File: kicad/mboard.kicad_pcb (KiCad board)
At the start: 2 copper layers, 3 parts

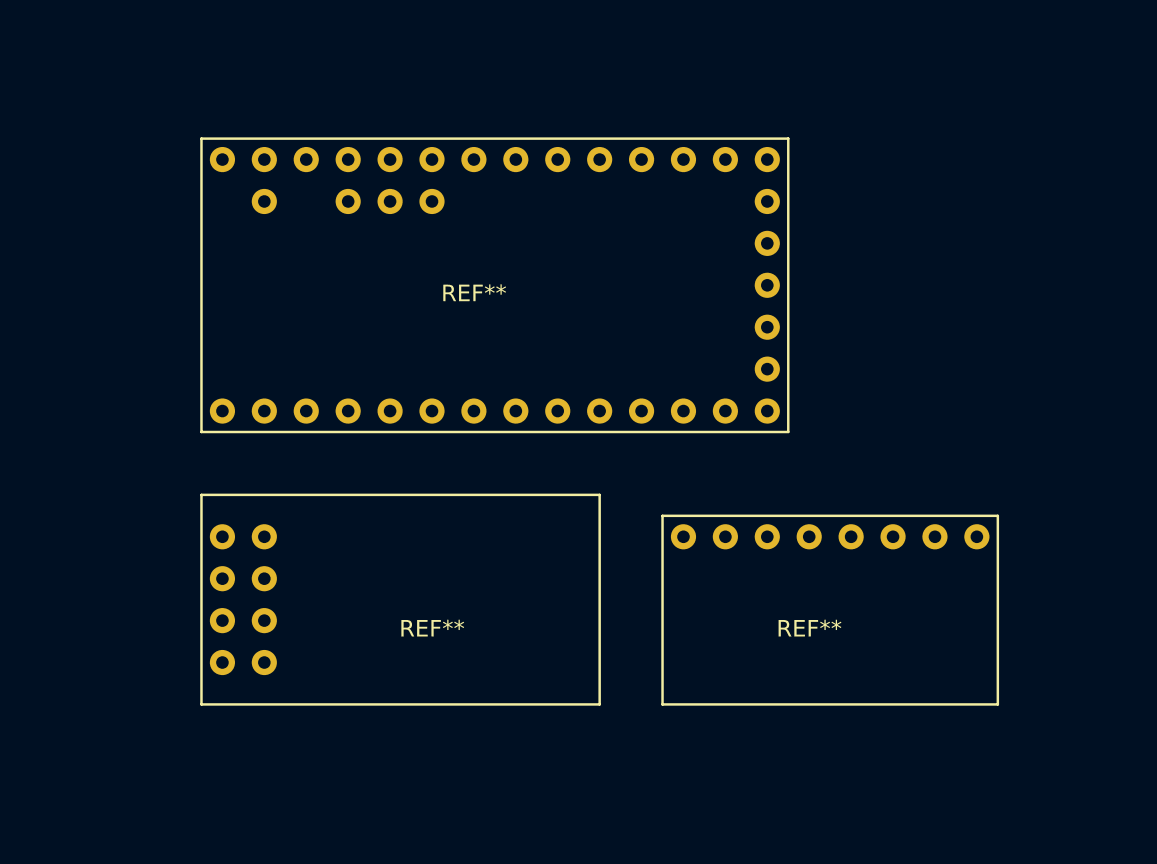
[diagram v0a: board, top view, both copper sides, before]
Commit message: add cut outline
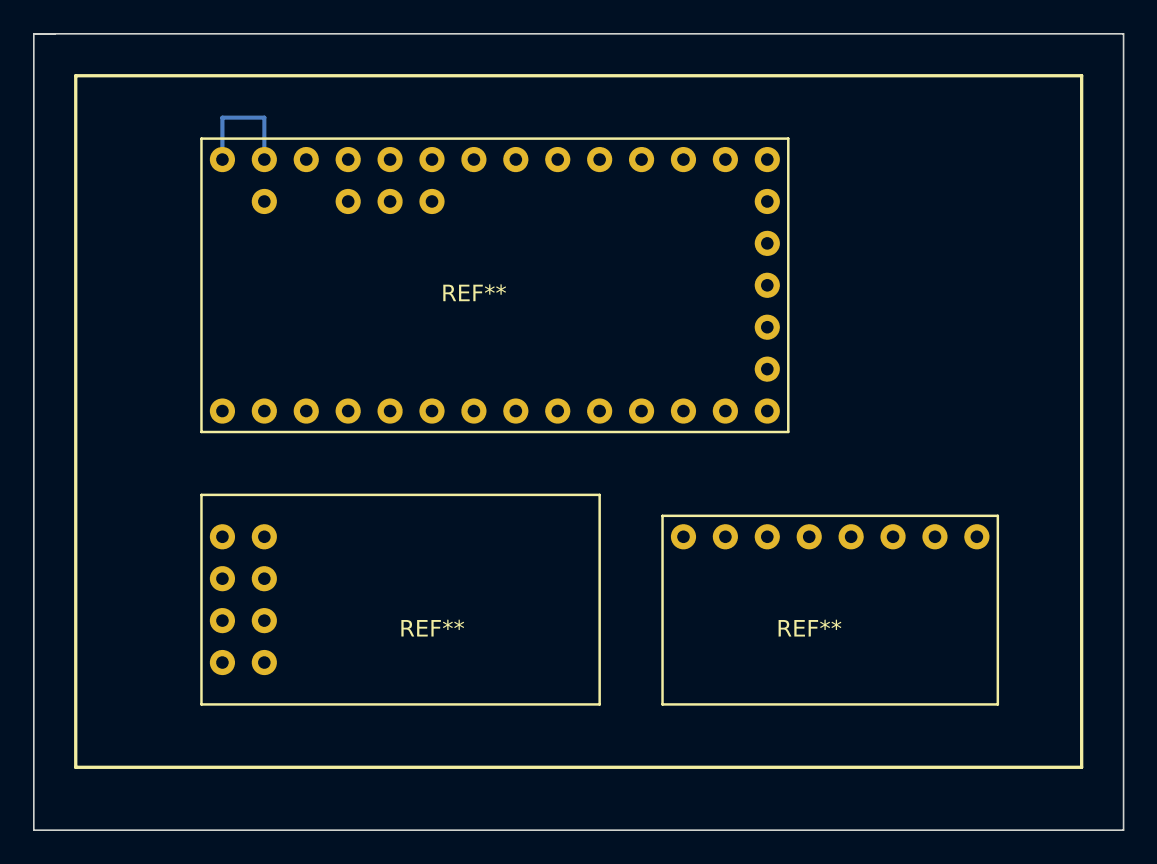
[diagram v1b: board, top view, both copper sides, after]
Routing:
- net (no net): track 0.00 -> 7.62 mm
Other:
- board outline added: 66 x 48.3 mm
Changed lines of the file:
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@@
     (links 0)
     (no_connects 0)
-    (area 35.284999 41.634999 84.095001 76.475001)
+    (area 25.349999 35.509999 91.490001 83.870001)
     (thickness 1.6)
-    (drawings 0)
-    (tracks 0)
+    (drawings 9)
+    (tracks 3)
     (zones 0)
     (modules 3)
@@
     (visible_elements FFFFFF7F)
     (pcbplotparams
-      (layerselection 0x00030_80000001)
-      (usegerberextensions false)
+      (layerselection 0x010f0_80000001)
+      (usegerberextensions true)
       (excludeedgelayer true)
       (linewidth 0.100000)
@@
       (outputformat 1)
       (mirror false)
-      (drillshape 1)
+      (drillshape 0)
       (scaleselection 1)
-      (outputdirectory ""))
+      (outputdirectory /tmp/w))
   )
   (net 0 "")
@@
     (pad 4 thru_hole circle (at -2.54 -5.08) (size 1.524 1.524) (drill 0.762) (layers *.Cu *.Mask F.SilkS))
   )
+  (gr_line (start 25.4 35.56) (end 26.67 35.56) (angle 90) (layer Edge.Cuts) (width 0.1))
+  (gr_line (start 25.4 83.82) (end 25.4 35.56) (angle 90) (layer Edge.Cuts) (width 0.1))
+  (gr_line (start 91.44 83.82) (end 25.4 83.82) (angle 90) (layer Edge.Cuts) (width 0.1))
+  (gr_line (start 91.44 35.56) (end 91.44 83.82) (angle 90) (layer Edge.Cuts) (width 0.1))
+  (gr_line (start 25.4 35.56) (end 91.44 35.56) (angle 90) (layer Edge.Cuts) (width 0.1))
+  (gr_line (start 88.9 38.1) (end 27.94 38.1) (angle 90) (layer F.SilkS) (width 0.2))
+  (gr_line (start 88.9 80.01) (end 88.9 38.1) (angle 90) (layer F.SilkS) (width 0.2))
+  (gr_line (start 27.94 80.01) (end 88.9 80.01) (angle 90) (layer F.SilkS) (width 0.2))
+  (gr_line (start 27.94 38.1) (end 27.94 80.01) (angle 90) (layer F.SilkS) (width 0.2))
+  (segment (start 36.83 43.18) (end 36.83 40.64) (width 0.25) (layer B.Cu) (net 0) (status 400000))
+  (segment (start 39.37 40.64) (end 39.37 43.18) (width 0.25) (layer B.Cu) (net 0) (status 800000))
+  (segment (start 36.83 40.64) (end 39.37 40.64) (width 0.25) (layer B.Cu) (net 0))
 )

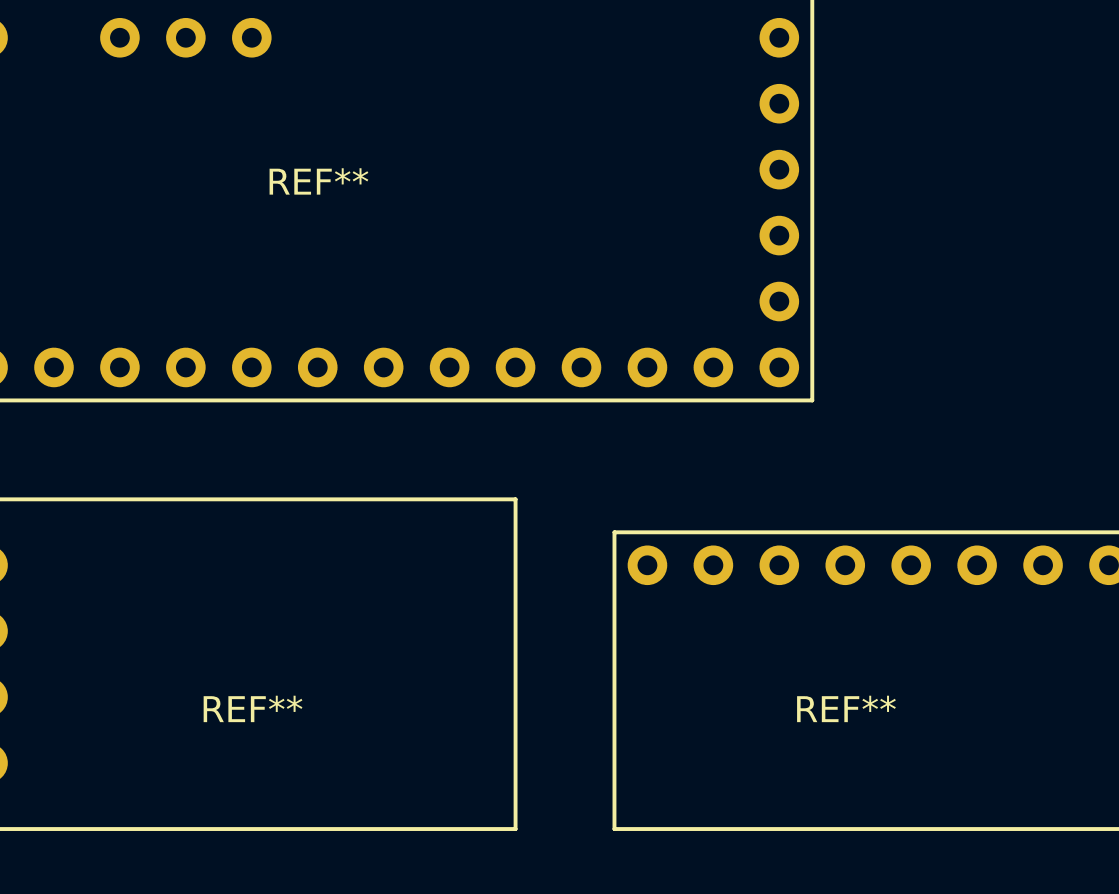
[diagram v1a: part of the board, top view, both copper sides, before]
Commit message: actual REF names
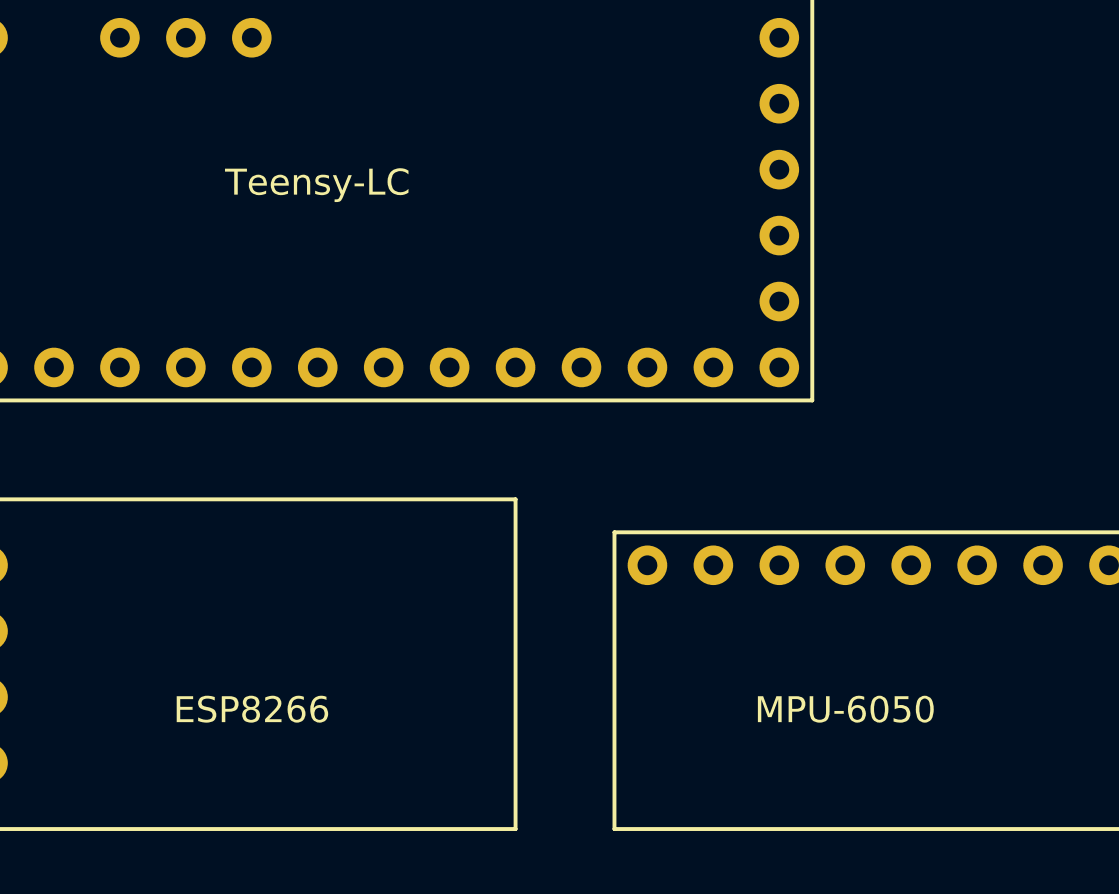
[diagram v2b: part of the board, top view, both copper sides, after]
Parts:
- renumbered REF** to ESP8266, REF** to MPU-6050, REF** to Teensy-LC
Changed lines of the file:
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@@
   (module modules:ESP8266 (layer F.Cu)
     (at 49.53 71.12)
-    (fp_text reference REF** (at 0 0.5) (layer F.SilkS)
+    (fp_text reference ESP8266 (at 0 0.5) (layer F.SilkS)
       (effects (font (size 1 1) (thickness 0.15)))
     )
@@
   (module modules:MPU6050 (layer F.Cu)
     (at 72.39 71.12)
-    (fp_text reference REF** (at 0 0.5) (layer F.SilkS)
+    (fp_text reference MPU-6050 (at 0 0.5) (layer F.SilkS)
       (effects (font (size 1 1) (thickness 0.15)))
     )
@@
   (module modules:Teensy-LC (layer F.Cu)
     (at 52.07 50.8)
-    (fp_text reference REF** (at 0 0.5) (layer F.SilkS)
+    (fp_text reference Teensy-LC (at 0 0.5) (layer F.SilkS)
       (effects (font (size 1 1) (thickness 0.15)))
     )
@@
   (gr_line (start 27.94 80.01) (end 88.9 80.01) (angle 90) (layer F.SilkS) (width 0.2))
   (gr_line (start 27.94 38.1) (end 27.94 80.01) (angle 90) (layer F.SilkS) (width 0.2))
-  (segment (start 36.83 43.18) (end 36.83 40.64) (width 0.25) (layer B.Cu) (net 0) (status 400000))
-  (segment (start 39.37 40.64) (end 39.37 43.18) (width 0.25) (layer B.Cu) (net 0) (status 800000))
   (segment (start 36.83 40.64) (end 39.37 40.64) (width 0.25) (layer B.Cu) (net 0))
+  (segment (start 39.37 40.64) (end 39.37 43.18) (width 0.25) (layer B.Cu) (net 0))
+  (segment (start 36.83 43.18) (end 36.83 40.64) (width 0.25) (layer B.Cu) (net 0))
 )

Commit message: mpu6050 thin
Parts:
- MPU-6050: footprint modules:MPU6050 -> modules:MPU6050-thin
- moved MPU-6050 8.03 mm to (74.9, 63.5), turned to 90 degrees
- moved Teensy-LC 6.84 mm to (45.7, 48.3)
- moved ESP8266 3.59 mm to (47.0, 68.6)
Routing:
- net (no net): track 7.62 -> 171.2 mm, vias 0 -> 5
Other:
- board size 66 x 48.3 mm -> 49.5 x 40.6 mm
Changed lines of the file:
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@@
     (links 0)
     (no_connects 0)
-    (area 25.349999 35.509999 91.490001 83.870001)
+    (area 25.349999 35.509999 74.980001 76.250001)
     (thickness 1.6)
-    (drawings 9)
-    (tracks 3)
+    (drawings 4)
+    (tracks 30)
     (zones 0)
     (modules 3)
@@
     (pad_to_mask_clearance 0)
     (aux_axis_origin 0 0)
-    (visible_elements FFFFFF7F)
+    (visible_elements FFFFF77F)
     (pcbplotparams
       (layerselection 0x010f0_80000001)
@@
   )
   (module modules:ESP8266 (layer F.Cu)
-    (at 49.53 71.12)
+    (at 46.99 68.58)
     (fp_text reference ESP8266 (at 0 0.5) (layer F.SilkS)
       (effects (font (size 1 1) (thickness 0.15)))
@@
     (pad 9 thru_hole circle (at -10.16 -5.08) (size 1.524 1.524) (drill 0.762) (layers *.Cu *.Mask F.SilkS))
   )
-  (module modules:MPU6050 (layer F.Cu)
-    (at 72.39 71.12)
-    (fp_text reference MPU-6050 (at 0 0.5) (layer F.SilkS)
-      (effects (font (size 1 1) (thickness 0.15)))
-    )
-    (fp_text value MPU6050 (at 0 -0.5) (layer F.Fab)
-      (effects (font (size 1 1) (thickness 0.15)))
-    )
-    (fp_line (start -8.89 -6.35) (end 11.43 -6.35) (layer F.SilkS) (width 0.15))
-    (fp_line (start 11.43 -6.35) (end 11.43 5.08) (layer F.SilkS) (width 0.15))
-    (fp_line (start 11.43 5.08) (end -8.89 5.08) (layer F.SilkS) (width 0.15))
-    (fp_line (start -8.89 5.08) (end -8.89 -6.35) (layer F.SilkS) (width 0.15))
-    (pad 1 thru_hole circle (at -7.62 -5.08) (size 1.524 1.524) (drill 0.762) (layers *.Cu *.Mask F.SilkS))
-    (pad 2 thru_hole circle (at -5.08 -5.08) (size 1.524 1.524) (drill 0.762) (layers *.Cu *.Mask F.SilkS))
-    (pad 3 thru_hole circle (at -2.54 -5.08) (size 1.524 1.524) (drill 0.762) (layers *.Cu *.Mask F.SilkS))
-    (pad 4 thru_hole circle (at 0 -5.08) (size 1.524 1.524) (drill 0.762) (layers *.Cu *.Mask F.SilkS))
-    (pad 5 thru_hole circle (at 2.54 -5.08) (size 1.524 1.524) (drill 0.762) (layers *.Cu *.Mask F.SilkS))
-    (pad 6 thru_hole circle (at 5.08 -5.08) (size 1.524 1.524) (drill 0.762) (layers *.Cu *.Mask F.SilkS))
-    (pad 7 thru_hole circle (at 7.62 -5.08) (size 1.524 1.524) (drill 0.762) (layers *.Cu *.Mask F.SilkS))
-    (pad 8 thru_hole circle (at 10.16 -5.08) (size 1.524 1.524) (drill 0.762) (layers *.Cu *.Mask F.SilkS))
-  )
   (module modules:Teensy-LC (layer F.Cu)
-    (at 52.07 50.8)
+    (at 45.72 48.26)
     (fp_text reference Teensy-LC (at 0 0.5) (layer F.SilkS)
       (effects (font (size 1 1) (thickness 0.15)))
@@
     (pad 4 thru_hole circle (at -2.54 -5.08) (size 1.524 1.524) (drill 0.762) (layers *.Cu *.Mask F.SilkS))
   )
-  (gr_line (start 25.4 35.56) (end 26.67 35.56) (angle 90) (layer Edge.Cuts) (width 0.1))
-  (gr_line (start 25.4 83.82) (end 25.4 35.56) (angle 90) (layer Edge.Cuts) (width 0.1))
-  (gr_line (start 91.44 83.82) (end 25.4 83.82) (angle 90) (layer Edge.Cuts) (width 0.1))
-  (gr_line (start 91.44 35.56) (end 91.44 83.82) (angle 90) (layer Edge.Cuts) (width 0.1))
-  (gr_line (start 25.4 35.56) (end 91.44 35.56) (angle 90) (layer Edge.Cuts) (width 0.1))
-  (gr_line (start 88.9 38.1) (end 27.94 38.1) (angle 90) (layer F.SilkS) (width 0.2))
-  (gr_line (start 88.9 80.01) (end 88.9 38.1) (angle 90) (layer F.SilkS) (width 0.2))
-  (gr_line (start 27.94 80.01) (end 88.9 80.01) (angle 90) (layer F.SilkS) (width 0.2))
-  (gr_line (start 27.94 38.1) (end 27.94 80.01) (angle 90) (layer F.SilkS) (width 0.2))
-  (segment (start 36.83 40.64) (end 39.37 40.64) (width 0.25) (layer B.Cu) (net 0))
-  (segment (start 39.37 40.64) (end 39.37 43.18) (width 0.25) (layer B.Cu) (net 0))
-  (segment (start 36.83 43.18) (end 36.83 40.64) (width 0.25) (layer B.Cu) (net 0))
+  (module modules:MPU6050-thin (layer F.Cu)
+    (at 74.93 63.5 90)
+    (fp_text reference MPU-6050 (at 3.81 -3.81 90) (layer F.SilkS)
+      (effects (font (size 1 1) (thickness 0.15)))
+    )
+    (fp_text value MPU6050 (at -5.08 -3.81 90) (layer F.Fab)
+      (effects (font (size 1 1) (thickness 0.15)))
+    )
+    (fp_line (start -8.89 -6.35) (end 11.43 -6.35) (layer F.SilkS) (width 0.15))
+    (fp_line (start 11.43 -2.54) (end -8.89 -2.54) (layer F.SilkS) (width 0.15))
+    (pad 1 thru_hole circle (at -7.62 -5.08 90) (size 1.524 1.524) (drill 0.762) (layers *.Cu *.Mask F.SilkS))
+    (pad 2 thru_hole circle (at -5.08 -5.08 90) (size 1.524 1.524) (drill 0.762) (layers *.Cu *.Mask F.SilkS))
+    (pad 3 thru_hole circle (at -2.54 -5.08 90) (size 1.524 1.524) (drill 0.762) (layers *.Cu *.Mask F.SilkS))
+    (pad 4 thru_hole circle (at 0 -5.08 90) (size 1.524 1.524) (drill 0.762) (layers *.Cu *.Mask F.SilkS))
+    (pad 5 thru_hole circle (at 2.54 -5.08 90) (size 1.524 1.524) (drill 0.762) (layers *.Cu *.Mask F.SilkS))
+    (pad 6 thru_hole circle (at 5.08 -5.08 90) (size 1.524 1.524) (drill 0.762) (layers *.Cu *.Mask F.SilkS))
+    (pad 7 thru_hole circle (at 7.62 -5.08 90) (size 1.524 1.524) (drill 0.762) (layers *.Cu *.Mask F.SilkS))
+    (pad 8 thru_hole circle (at 10.16 -5.08 90) (size 1.524 1.524) (drill 0.762) (layers *.Cu *.Mask F.SilkS))
+  )
+  (gr_line (start 74.93 76.2) (end 25.4 76.2) (angle 90) (layer Edge.Cuts) (width 0.1))
+  (gr_line (start 74.93 35.56) (end 74.93 76.2) (angle 90) (layer Edge.Cuts) (width 0.1))
+  (gr_line (start 25.4 35.56) (end 74.93 35.56) (angle 90) (layer Edge.Cuts) (width 0.1))
+  (gr_line (start 25.4 35.56) (end 25.4 76.2) (angle 90) (layer Edge.Cuts) (width 0.1))
+  (segment (start 31.75 66.04) (end 31.75 71.12) (width 0.25) (layer B.Cu) (net 0))
+  (segment (start 31.75 66.04) (end 30.48 66.04) (width 0.25) (layer B.Cu) (net 0))
+  (via (at 30.48 66.04) (size 0.6) (layers F.Cu B.Cu) (net 0))
+  (via (at 30.48 68.58) (size 0.6) (layers F.Cu B.Cu) (net 0))
+  (segment (start 29.21 68.58) (end 30.48 68.58) (width 0.25) (layer B.Cu) (net 0))
+  (segment (start 29.21 62.23) (end 29.21 68.58) (width 0.25) (layer B.Cu) (net 0))
+  (segment (start 34.29 71.12) (end 31.75 71.12) (width 0.25) (layer B.Cu) (net 0))
+  (via (at 30.48 71.12) (size 0.6) (layers F.Cu B.Cu) (net 0))
+  (segment (start 30.48 71.12) (end 27.94 71.12) (width 0.25) (layer F.Cu) (net 0))
+  (via (at 27.94 53.34) (size 0.6) (layers F.Cu B.Cu) (net 0))
+  (segment (start 27.94 53.34) (end 30.48 55.88) (width 0.25) (layer B.Cu) (net 0))
+  (segment (start 27.94 50.8) (end 26.67 50.8) (width 0.25) (layer F.Cu) (net 0))
+  (segment (start 30.48 40.64) (end 27.94 40.64) (width 0.25) (layer F.Cu) (net 0))
+  (segment (start 27.94 40.64) (end 27.94 50.8) (width 0.25) (layer F.Cu) (net 0))
+  (via (at 27.94 50.8) (size 0.6) (layers F.Cu B.Cu) (net 0))
+  (segment (start 27.94 55.88) (end 27.94 59.69) (width 0.25) (layer F.Cu) (net 0))
+  (segment (start 26.67 55.88) (end 27.94 55.88) (width 0.25) (layer F.Cu) (net 0))
+  (segment (start 26.67 50.8) (end 26.67 55.88) (width 0.25) (layer F.Cu) (net 0))
+  (segment (start 30.48 59.69) (end 30.48 62.23) (width 0.25) (layer B.Cu) (net 0))
+  (segment (start 30.48 62.23) (end 29.21 62.23) (width 0.25) (layer B.Cu) (net 0))
+  (segment (start 27.94 71.12) (end 27.94 59.69) (width 0.25) (layer F.Cu) (net 0))
+  (segment (start 36.83 59.69) (end 36.83 63.5) (width 0.25) (layer B.Cu) (net 0))
+  (segment (start 30.48 59.69) (end 36.83 59.69) (width 0.25) (layer B.Cu) (net 0))
+  (segment (start 36.83 59.69) (end 55.88 59.69) (width 0.25) (layer B.Cu) (net 0))
+  (segment (start 55.88 68.58) (end 69.85 68.58) (width 0.25) (layer B.Cu) (net 0))
+  (segment (start 55.88 59.69) (end 55.88 68.58) (width 0.25) (layer B.Cu) (net 0))
+  (segment (start 30.48 55.88) (end 30.48 59.69) (width 0.25) (layer B.Cu) (net 0))
+  (segment (start 27.94 59.69) (end 55.88 59.69) (width 0.25) (layer F.Cu) (net 0))
+  (segment (start 55.88 71.12) (end 69.85 71.12) (width 0.25) (layer F.Cu) (net 0))
+  (segment (start 55.88 59.69) (end 55.88 71.12) (width 0.25) (layer F.Cu) (net 0))
 )
